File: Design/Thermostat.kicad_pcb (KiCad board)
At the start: 2 copper layers, 54.6 x 71.8 mm, 31 parts, among them J1 BARREL_JACK, J2 CONN_01X01_MALE, J3 CONN_01X01_MALE, J4 CONN_01X01_MALE, J5 CONN_01X01_MALE, J6 CONN_01X01_MALE, J7 CONN_01X01_MALE, J8 Screw_Terminal_1x03, Q1 BC547, SW1 SW_Push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

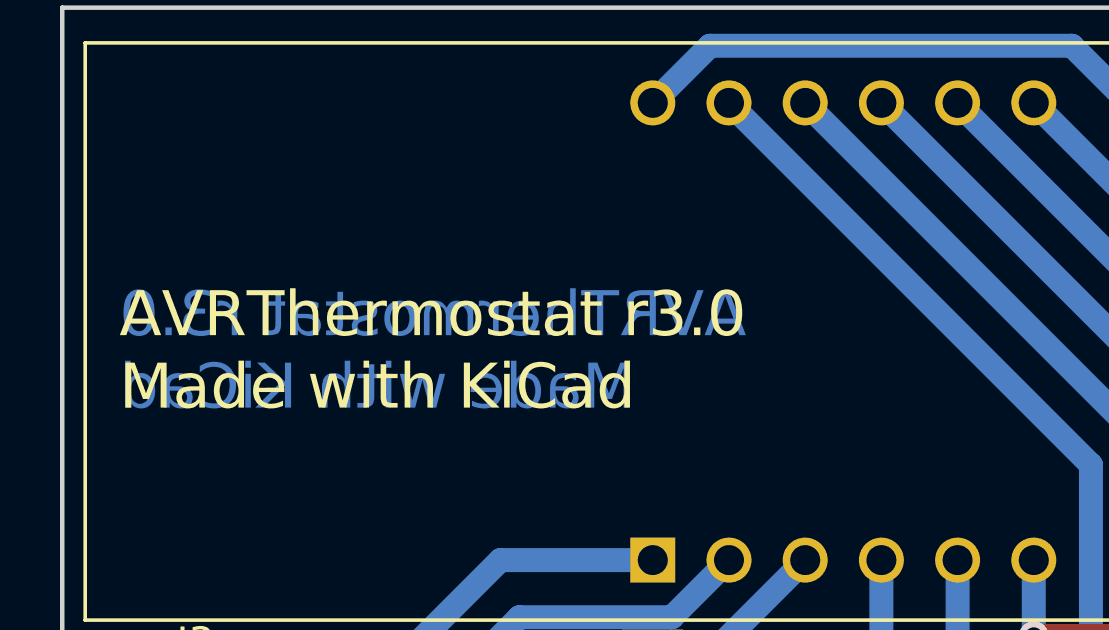
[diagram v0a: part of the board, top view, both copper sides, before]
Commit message: Add a recommendation to enabling the BOD
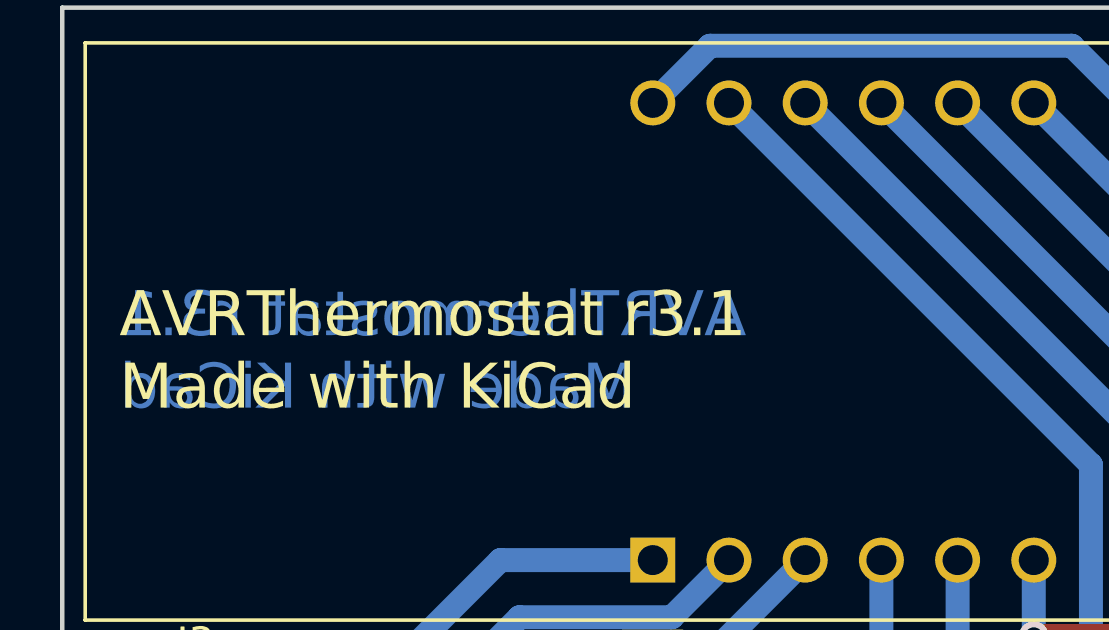
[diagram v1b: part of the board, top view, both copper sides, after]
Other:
- board text added: "AVRThermostat r3.1 Made with KiCad"
- board text removed: "AVRThermostat r3.0 Made with KiCad"
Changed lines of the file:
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@@
   (title_block
     (title "Thermostat on ATmega8A, DS18B20 and 7-segment Display")
-    (date 2017-07-30)
-    (rev 3.0)
+    (date 2017-10-07)
+    (rev 3.1)
     (company "Artyom Protaskin")
   )
@@
     )
   )
-  (gr_text "AVRThermostat r3.0\nMade with KiCad" (at 121.92 70.485) (layer F.SilkS)
+  (gr_text "AVRThermostat r3.1\nMade with KiCad" (at 121.92 70.485) (layer F.SilkS)
     (effects (font (size 1.5 1.5) (thickness 0.3)) (justify left))
   )
-  (gr_text "AVRThermostat r3.0\nMade with KiCad" (at 121.92 70.485) (layer B.Cu)
+  (gr_text "AVRThermostat r3.1\nMade with KiCad" (at 121.92 70.485) (layer B.Cu)
     (effects (font (size 1.5 1.5) (thickness 0.3)) (justify right mirror))
   )
